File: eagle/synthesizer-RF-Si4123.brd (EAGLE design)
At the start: 45 x 38 mm, 47 parts, among them J1 142-0701-851, J2 142-0701-851, J3 142-0701-851, U1 LP38692, U2 SI4123, X1 ECS-TXO-3225

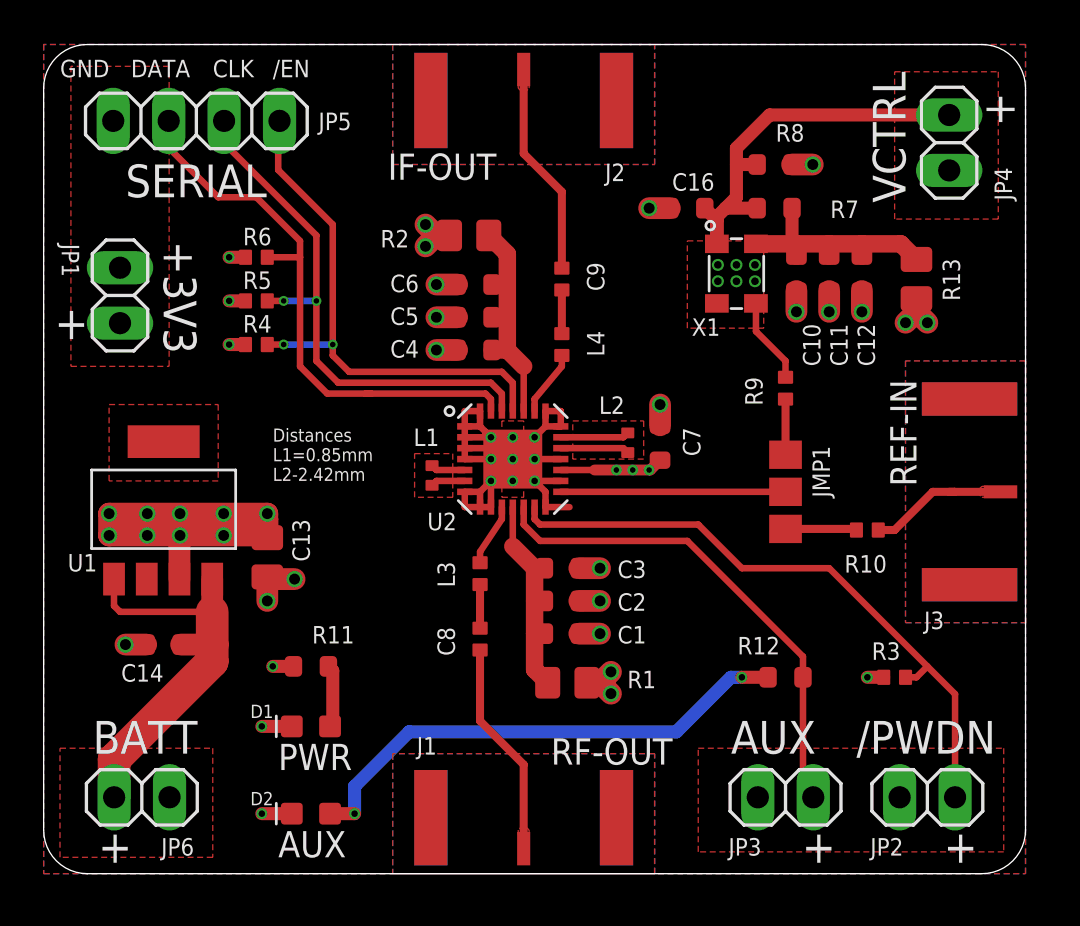
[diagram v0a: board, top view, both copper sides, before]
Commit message: Change resistor sizes. Add tstop to L1/2 traces.
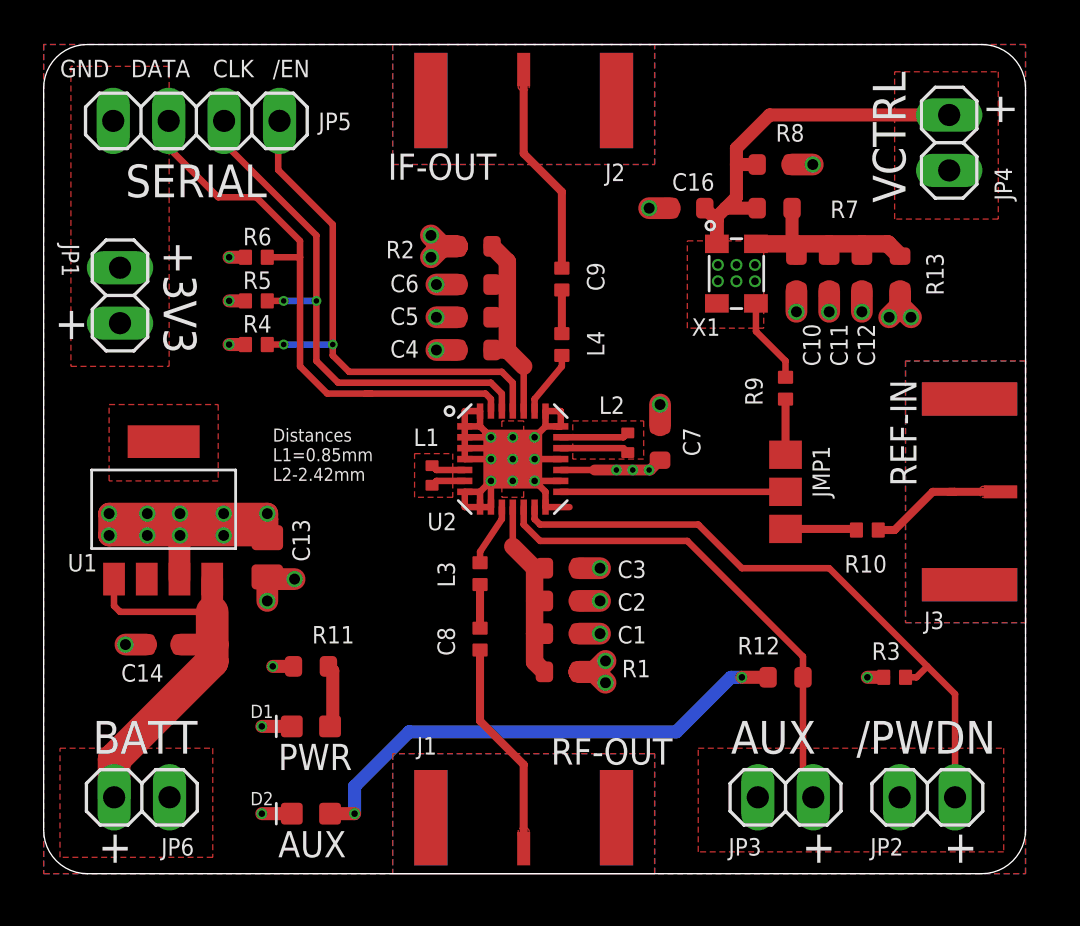
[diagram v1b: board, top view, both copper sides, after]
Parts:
- R1, R13, R2: device oresat-rcl:.0805-B-NOSILK -> oresat-rcl:.0603-B-NOSILK
- moved R13 0.79 mm to (39.2, 27.5)
- moved R1 0.56 mm to (23.8, 9.25)
- moved R2 0.56 mm to (19.8, 28.8)
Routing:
- net N$10: track 11.1 -> 10.3 mm
- net N$15: track 10.1 -> 9.50 mm
- net N$93: track 10.8 -> 10.3 mm
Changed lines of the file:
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@@
 <layer number="27" name="tValues" color="7" fill="1" visible="yes" active="yes"/>
 <layer number="28" name="bValues" color="7" fill="1" visible="no" active="yes"/>
-<layer number="29" name="tStop" color="7" fill="3" visible="no" active="yes"/>
+<layer number="29" name="tStop" color="7" fill="3" visible="yes" active="yes"/>
 <layer number="30" name="bStop" color="7" fill="6" visible="no" active="yes"/>
 <layer number="31" name="tCream" color="7" fill="4" visible="no" active="yes"/>
@@
 <layer number="43" name="vRestrict" color="2" fill="10" visible="yes" active="yes"/>
 <layer number="44" name="Drills" color="7" fill="1" visible="no" active="yes"/>
-<layer number="45" name="Holes" color="7" fill="1" visible="no" active="yes"/>
+<layer number="45" name="Holes" color="7" fill="1" visible="yes" active="yes"/>
 <layer number="46" name="Milling" color="3" fill="1" visible="no" active="yes"/>
 <layer number="47" name="Measures" color="7" fill="1" visible="no" active="yes"/>
@@
 2019-07-26 - Rev. 1
 E.M. KJ7AOG</text>
+<polygon width="0.3" layer="29">
+<vertex x="19.25" y="19"/>
+<vertex x="17.5" y="19"/>
+<vertex x="17.5" y="17.5"/>
+<vertex x="19.25" y="17.5"/>
+</polygon>
+<polygon width="0.3" layer="29">
+<vertex x="23.75" y="20.5"/>
+<vertex x="27.25" y="20.5"/>
+<vertex x="27.25" y="19"/>
+<vertex x="23.75" y="19"/>
+</polygon>
 </plain>
 <attributes>
@@
 <attribute name="NAME" x="23.75" y="24.25" size="0.2" layer="33" ratio="15" rot="R90" align="center"/>
 </element>
-<element name="R1" library="oresat-rcl" package=".0805-B-NOSILK" value="0" x="24" y="8.75" smashed="yes">
-<attribute name="NAME" x="26.75" y="8.5" size="0.8" layer="25" font="vector" ratio="15"/>
-<attribute name="NAME" x="24" y="8.75" size="0.4" layer="33" ratio="15" align="center"/>
+<element name="R1" library="oresat-rcl" package=".0603-B-NOSILK" value="0" x="23.75" y="9.25" smashed="yes">
+<attribute name="NAME" x="26.5" y="9" size="0.8" layer="25" font="vector" ratio="15"/>
+<attribute name="NAME" x="23.75" y="9.25" size="0.4" layer="33" ratio="15" align="center"/>
 </element>
 <element name="R10" library="oresat-rcl" package=".0402-B-NOSILK" value="0" x="37.75" y="15.75" smashed="yes">
@@
 <attribute name="NAME" x="34" y="9" size="0.3" layer="33" ratio="15" align="center"/>
 </element>
-<element name="R2" library="oresat-rcl" package=".0805-B-NOSILK" value="0" x="19.5" y="29.25" smashed="yes" rot="R180">
-<attribute name="NAME" x="16.75" y="29.5" size="0.8" layer="25" font="vector" ratio="15" rot="R180"/>
-<attribute name="NAME" x="19.5" y="29.25" size="0.4" layer="33" ratio="15" rot="R180" align="center"/>
+<element name="R2" library="oresat-rcl" package=".0603-B-NOSILK" value="0" x="19.75" y="28.75" smashed="yes" rot="R180">
+<attribute name="NAME" x="17" y="29" size="0.8" layer="25" font="vector" ratio="15" rot="R180"/>
+<attribute name="NAME" x="19.75" y="28.75" size="0.4" layer="33" ratio="15" rot="R180" align="center"/>
 </element>
 <element name="R3" library="oresat-rcl" package=".0402-B-NOSILK" value="47k" x="39" y="9" smashed="yes" rot="R180">
@@
 <attribute name="NAME" x="40.35" y="11.21" size="0.8" layer="25" font="vector" ratio="15"/>
 </element>
-<element name="R13" library="oresat-rcl" package=".0805-B-NOSILK" value="0" x="40" y="27.25" smashed="yes" rot="R90">
-<attribute name="NAME" x="42" y="26.25" size="0.8" layer="25" font="vector" ratio="15" rot="R90"/>
-<attribute name="NAME" x="40" y="27.25" size="0.4" layer="33" ratio="15" rot="R90" align="center"/>
+<element name="R13" library="oresat-rcl" package=".0603-B-NOSILK" value="0" x="39.25" y="27.5" smashed="yes" rot="R90">
+<attribute name="NAME" x="41.25" y="26.5" size="0.8" layer="25" font="vector" ratio="15" rot="R90"/>
+<attribute name="NAME" x="39.25" y="27.5" size="0.4" layer="33" ratio="15" rot="R90" align="center"/>
 </element>
 </elements>
@@
 <wire x1="21.25" y1="24" x2="21.25" y2="25.5" width="0.8" layer="1"/>
 <wire x1="21.25" y1="25.5" x2="21.25" y2="27" width="0.8" layer="1"/>
-<wire x1="21.25" y1="27" x2="21.25" y2="28.4" width="0.8" layer="1"/>
-<wire x1="21.25" y1="28.4" x2="20.4" y2="29.25" width="0.8" layer="1"/>
 <wire x1="20.55" y1="27" x2="21.25" y2="27" width="0.6" layer="1"/>
 <wire x1="20.55" y1="25.5" x2="21.25" y2="25.5" width="0.6" layer="1"/>
 <wire x1="20.55" y1="24" x2="21.25" y2="24" width="0.8" layer="1"/>
 <wire x1="21.25" y1="24" x2="22" y2="23.25" width="0.8" layer="1"/>
+<wire x1="20.55" y1="28.75" x2="21.25" y2="28.05" width="0.8" layer="1"/>
+<wire x1="21.25" y1="28.05" x2="21.25" y2="27" width="0.8" layer="1"/>
 </signal>
 <signal name="N$11" class="1">
@@
 <contactref element="R1" pad="1"/>
 <wire x1="22.5" y1="14" x2="22.5" y2="12.5" width="0.8" layer="1"/>
-<wire x1="22.5" y1="12.5" x2="22.5" y2="11" width="0.8" layer="1"/>
-<wire x1="22.5" y1="11" x2="22.5" y2="9.35" width="0.8" layer="1"/>
-<wire x1="22.5" y1="9.35" x2="23.1" y2="8.75" width="0.8" layer="1"/>
 <wire x1="22.95" y1="14" x2="22.5" y2="14" width="0.6" layer="1"/>
 <wire x1="22.95" y1="12.5" x2="22.5" y2="12.5" width="0.6" layer="1"/>
-<wire x1="22.95" y1="11" x2="22.5" y2="11" width="0.6" layer="1"/>
 <wire x1="21.5" y1="15" x2="21.5" y2="16.8" width="0.3" layer="1"/>
 <wire x1="22.5" y1="14" x2="21.5" y2="15" width="0.8" layer="1"/>
+<wire x1="22.95" y1="9.25" x2="22.5" y2="9.7" width="0.8" layer="1"/>
+<wire x1="22.5" y1="9.7" x2="22.5" y2="11" width="0.8" layer="1"/>
+<wire x1="22.5" y1="11" x2="22.5" y2="12.5" width="0.8" layer="1"/>
+<wire x1="22.95" y1="11" x2="22.5" y2="11" width="0.8" layer="1"/>
 </signal>
 <signal name="+3V3">
@@
 <vertex x="0" y="38"/>
 </polygon>
-<via x="17.5" y="29.75" extent="1-16" drill="0.5"/>
+<via x="17.75" y="29.25" extent="1-16" drill="0.5"/>
 <via x="8.5" y="24.25" extent="1-16" drill="0.3"/>
-<via x="26" y="8.25" extent="1-16" drill="0.5"/>
-<via x="26" y="9.25" extent="1-16" drill="0.5"/>
-<via x="17.5" y="28.75" extent="1-16" drill="0.5"/>
+<via x="25.75" y="8.75" extent="1-16" drill="0.5"/>
+<via x="25.75" y="9.75" extent="1-16" drill="0.5"/>
+<via x="17.75" y="28.25" extent="1-16" drill="0.5"/>
 <wire x1="38.5" y1="9" x2="37.75" y2="9" width="0.6" layer="1"/>
 <via x="37.75" y="9" extent="1-16" drill="0.3"/>
@@
 <wire x1="10.5" y1="9.5" x2="11.45" y2="9.5" width="0.6" layer="1"/>
 <contactref element="R13" pad="1"/>
-<via x="39.5" y="25.25" extent="1-16" drill="0.5"/>
-<via x="40.5" y="25.25" extent="1-16" drill="0.5"/>
-<wire x1="40" y1="26.35" x2="40" y2="25.75" width="1" layer="1"/>
-<wire x1="40" y1="25.75" x2="40.5" y2="25.25" width="1" layer="1"/>
-<wire x1="39.5" y1="25.25" x2="40" y2="25.75" width="1" layer="1"/>
+<via x="38.75" y="25.5" extent="1-16" drill="0.5"/>
+<via x="39.75" y="25.5" extent="1-16" drill="0.5"/>
+<wire x1="39.25" y1="26.7" x2="39.25" y2="26" width="1" layer="1"/>
+<wire x1="39.25" y1="26" x2="39.75" y2="25.5" width="1" layer="1"/>
+<wire x1="38.75" y1="25.5" x2="39.25" y2="26" width="1" layer="1"/>
 <wire x1="23.7" y1="18.5" x2="25.25" y2="18.5" width="0.3" layer="1"/>
 <wire x1="25.25" y1="18.5" x2="27.8" y2="18.5" width="0.5" layer="1"/>
-<wire x1="24.9" y1="8.75" x2="25.5" y2="8.75" width="1" layer="1"/>
-<wire x1="25.5" y1="8.75" x2="26" y2="9.25" width="1" layer="1"/>
-<wire x1="24.9" y1="8.75" x2="25.5" y2="8.75" width="1" layer="1"/>
-<wire x1="25.5" y1="8.75" x2="26" y2="8.25" width="1" layer="1"/>
-<wire x1="18.6" y1="29.25" x2="18" y2="29.25" width="1" layer="1"/>
-<wire x1="18" y1="29.25" x2="17.5" y2="29.75" width="1" layer="1"/>
-<wire x1="18.6" y1="29.25" x2="18" y2="29.25" width="1" layer="1"/>
-<wire x1="18" y1="29.25" x2="17.5" y2="28.75" width="1" layer="1"/>
+<wire x1="24.55" y1="9.25" x2="25.25" y2="9.25" width="1" layer="1"/>
+<wire x1="25.25" y1="9.25" x2="25.75" y2="9.75" width="1" layer="1"/>
+<wire x1="24.55" y1="9.25" x2="25.25" y2="9.25" width="1" layer="1"/>
+<wire x1="25.25" y1="9.25" x2="25.75" y2="8.75" width="1" layer="1"/>
+<wire x1="18.95" y1="28.75" x2="18.25" y2="28.75" width="1" layer="1"/>
+<wire x1="18.25" y1="28.75" x2="17.75" y2="29.25" width="1" layer="1"/>
+<wire x1="18.95" y1="28.75" x2="18.25" y2="28.75" width="1" layer="1"/>
+<wire x1="18.25" y1="28.75" x2="17.75" y2="28.25" width="1" layer="1"/>
 <wire x1="27.75" y1="18.5" x2="27.8" y2="18.5" width="0" layer="19" extent="1-1"/>
 </signal>
@@
 <contactref element="R13" pad="2"/>
 <contactref element="R7" pad="2"/>
-<wire x1="40" y1="28.15" x2="39.285" y2="28.865" width="0.8" layer="1"/>
-<wire x1="39.285" y1="28.865" x2="37.5" y2="28.865" width="0.8" layer="1"/>
 <wire x1="37.5" y1="28.865" x2="36" y2="28.865" width="0.8" layer="1"/>
 <wire x1="36" y1="28.865" x2="34.5" y2="28.865" width="0.8" layer="1"/>
@@
 <wire x1="34.3" y1="30.5" x2="34.3" y2="29.065" width="0.6" layer="1"/>
 <wire x1="34.3" y1="29.065" x2="34.5" y2="28.865" width="0.6" layer="1"/>
+<wire x1="39.25" y1="28.3" x2="38.685" y2="28.865" width="0.8" layer="1"/>
+<wire x1="38.685" y1="28.865" x2="37.5" y2="28.865" width="0.8" layer="1"/>
 </signal>
 </signals>

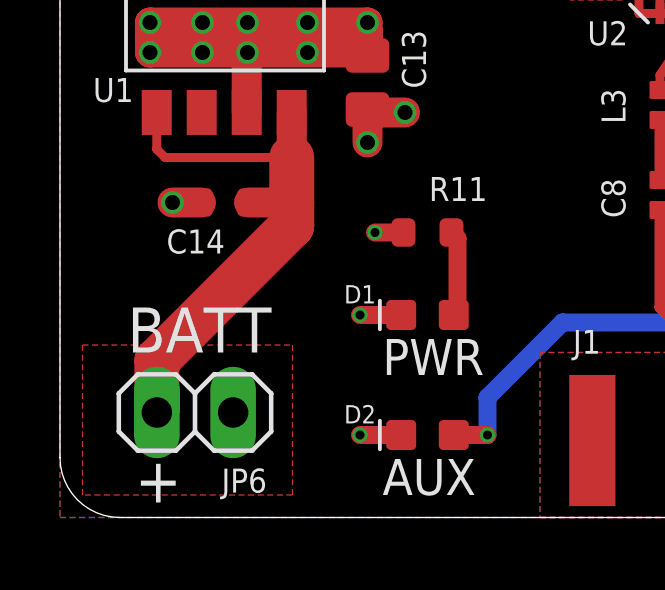
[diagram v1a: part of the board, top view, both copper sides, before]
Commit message: Flip batt header
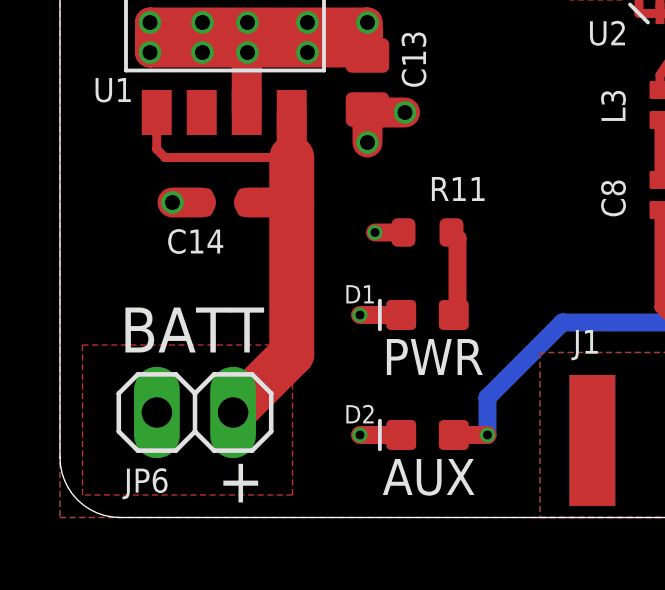
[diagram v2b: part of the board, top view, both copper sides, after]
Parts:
- turned JP6 to 0 degrees
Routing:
- net +BAT: track 19.1 -> 18.1 mm
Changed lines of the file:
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@@
 L1=0.85mm
 L2-2.42mm</text>
-<text x="2.25" y="5.5" size="1.5" layer="21" font="vector" ratio="15">BATT</text>
-<text x="2.5" y="0.5" size="1.5" layer="21" font="vector" ratio="15">+</text>
+<text x="2" y="5.5" size="1.5" layer="21" font="vector" ratio="15">BATT</text>
+<text x="5.25" y="0.5" size="1.5" layer="21" font="vector" ratio="15">+</text>
 <text x="34.75" y="0.5" size="1.5" layer="21" font="vector" ratio="15">+</text>
 <text x="41.25" y="0.5" size="1.5" layer="21" font="vector" ratio="15">+</text>
@@
 <attribute name="VALUE" x="1.92" y="31.325" size="1.27" layer="27"/>
 </element>
-<element name="JP6" library="pinhead" library_urn="urn:adsk.eagle:library:325" package="1X02" package3d_urn="urn:adsk.eagle:package:22435/2" value="" x="4.5" y="3.5" smashed="yes" rot="R180">
-<attribute name="NAME" x="5.3838" y="0.8288" size="0.8" layer="25" font="vector" ratio="15"/>
-<attribute name="POPULARITY" value="98" x="4.5" y="3.5" size="1.778" layer="27" rot="R180" display="off"/>
-<attribute name="VALUE" x="7.04" y="6.675" size="1.27" layer="27" rot="R180"/>
+<element name="JP6" library="pinhead" library_urn="urn:adsk.eagle:library:325" package="1X02" package3d_urn="urn:adsk.eagle:package:22435/2" value="" x="4.5" y="3.5" smashed="yes">
+<attribute name="NAME" x="2.1338" y="0.8288" size="0.8" layer="25" font="vector" ratio="15"/>
+<attribute name="POPULARITY" value="98" x="4.5" y="3.5" size="1.778" layer="27" display="off"/>
+<attribute name="VALUE" x="1.96" y="0.325" size="1.27" layer="27"/>
 </element>
 <element name="L1" library="oresat-rcl" package=".0402-C-NOSILK" value="1.8n" x="17.8" y="18.25" smashed="yes" rot="R270">
@@
 <wire x1="7.725" y1="13.5" x2="7.725" y2="12" width="1" layer="1"/>
 <wire x1="7.725" y1="12" x2="7.725" y2="10.5" width="1.5" layer="1"/>
-<wire x1="7.725" y1="10.5" x2="7.725" y2="9.725" width="1.5" layer="1"/>
-<wire x1="3.23" y1="5.23" x2="3.23" y2="3.5" width="1.5" layer="1"/>
-<wire x1="7.725" y1="9.725" x2="3.23" y2="5.23" width="1.5" layer="1"/>
 <wire x1="3.225" y1="13.5" x2="3.225" y2="12.275" width="0.3" layer="1"/>
 <wire x1="3.225" y1="12.275" x2="3.5" y2="12" width="0.3" layer="1"/>
 <wire x1="3.5" y1="12" x2="7.725" y2="12" width="0.3" layer="1"/>
 <wire x1="6.3" y1="10.5" x2="7.725" y2="10.5" width="1" layer="1"/>
+<wire x1="5.77" y1="3.5" x2="7.725" y2="5.455" width="1.5" layer="1"/>
+<wire x1="7.725" y1="5.455" x2="7.725" y2="10.5" width="1.5" layer="1"/>
 </signal>
 <signal name="N$21">

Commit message: Added stitching
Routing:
- net GND: vias 32 -> 270
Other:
- board text added: "Dual RF Synthesizer 436.5 / 1265 MHz 2019-07-29 Rev. 1 E.M. KJ7AOG"
- board text removed: "Dual RF Synthesizer 436.5 / 1265 MHz 2019-07-26 - Rev. 1 E.M. KJ7AOG"

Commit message: Update cap values
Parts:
- C10: value 22n -> 1u
- C13: value 4.7u -> 10u
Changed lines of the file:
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@@
 <drawing>
 <settings>
-<setting alwaysvectorfont="yes"/>
+<setting alwaysvectorfont="no"/>
 <setting verticaltext="up"/>
 </settings>
-<grid distance="0.25" unitdist="mm" unit="mm" style="lines" multiple="4" display="yes" altdistance="0.1" altunitdist="mm" altunit="mm"/>
+<grid distance="0.25" unitdist="mm" unit="mm" style="lines" multiple="4" display="yes" altdistance="0.01" altunitdist="mm" altunit="mm"/>
 <layers>
 <layer number="1" name="Top" color="4" fill="1" visible="yes" active="yes"/>
@@
 <attribute name="NAME" x="23.75" y="11" size="0.3" layer="33" ratio="15" align="center"/>
 </element>
-<element name="C10" library="oresat-rcl" package=".0603-B-NOSILK" value="22n" x="34.5" y="27.5" smashed="yes" rot="R270">
+<element name="C10" library="oresat-rcl" package=".0603-B-NOSILK" value="1u" x="34.5" y="27.5" smashed="yes" rot="R270">
 <attribute name="NAME" x="34.8" y="25.2" size="0.8" layer="25" font="vector" ratio="15" rot="R270"/>
 <attribute name="NAME" x="34.5" y="27.5" size="0.3" layer="33" ratio="15" rot="R270" align="center"/>
@@
 <attribute name="NAME" x="37.5" y="27.5" size="0.3" layer="33" ratio="15" rot="R270" align="center"/>
 </element>
-<element name="C13" library="oresat-rcl" package=".0805-B-NOSILK" value="4.7u" x="10.25" y="14.5" smashed="yes" rot="R270">
+<element name="C13" library="oresat-rcl" package=".0805-B-NOSILK" value="10u" x="10.25" y="14.5" smashed="yes" rot="R270">
 <attribute name="NAME" x="12.2" y="14.3" size="0.8" layer="25" font="vector" ratio="15" rot="R90"/>
 <attribute name="NAME" x="10.25" y="14.5" size="0.3" layer="33" ratio="15" rot="R270" align="center"/>

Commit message: Update LED resistor
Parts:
- R12: value 3.3k -> 2.7k
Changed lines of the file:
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@@
 <attribute name="NAME" x="12.25" y="9.5" size="0.3" layer="33" ratio="15" rot="R180" align="center"/>
 </element>
-<element name="R12" library="oresat-rcl" package=".0603-B-NOSILK" value="3.3k" x="34" y="9" smashed="yes">
+<element name="R12" library="oresat-rcl" package=".0603-B-NOSILK" value="2.7k" x="34" y="9" smashed="yes">
 <attribute name="NAME" x="31.8" y="10.05" size="0.8" layer="25" font="vector" ratio="15"/>
 <attribute name="NAME" x="34" y="9" size="0.3" layer="33" ratio="15" align="center"/>
